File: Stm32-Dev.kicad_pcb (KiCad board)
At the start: 2 copper layers, 33 x 92.7 mm, 37 parts, among them J2 STDC14, U1 STM32F405RGTx, U2 TPS63070RNMR, X1 25MHz

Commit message: PCB ready for routing
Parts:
- moved S2 0.86 mm to (159.2, 86.2)
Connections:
- S2 pad S1: (no net) -> GND
- S2 pad S2: (no net) -> GND
- S2 pad S3: (no net) -> GND
- S2 pad S4: (no net) -> GND
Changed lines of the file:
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@@
   )
   (footprint "EG1215AA:SW_EG1215AA" (layer "F.Cu")
-    (at 160.02 86.13 -90)
+    (at 159.165 86.2 -90)
     (property "MANUFACTURER" "E Switch")
     (property "MAXIMUM_PACKAGE_HEIGHT" "1.40mm")
@@
     (property "Sheetname" "")
     (attr smd)
-    (fp_text reference "S2" (at -1.225 -4.131 -90) (layer "F.SilkS")
+    (fp_text reference "S2" (at -1.225 -4.131 90) (layer "F.SilkS")
         (effects (font (size 1 1) (thickness 0.15)))
     )
-    (fp_text value "BOOT0" (at 2.585 4.077 -90) (layer "F.Fab")
+    (fp_text value "BOOT0" (at 2.585 4.077 90) (layer "F.Fab")
         (effects (font (size 1 1) (thickness 0.15)))
     )
@@
     (pad "3" smd rect (at 2.25 -1.75 270) (size 0.7 1.5) (layers "F.Cu" "F.Paste" "F.Mask")
       (net 2 "GND") (pintype "passive"))
-    (pad "S1" smd rect (at -3.65 -1.05 270) (size 1 0.8) (layers "F.Cu" "F.Paste" "F.Mask"))
-    (pad "S2" smd rect (at -3.65 1.05 270) (size 1 0.8) (layers "F.Cu" "F.Paste" "F.Mask"))
-    (pad "S3" smd rect (at 3.65 1.05 270) (size 1 0.8) (layers "F.Cu" "F.Paste" "F.Mask"))
-    (pad "S4" smd rect (at 3.65 -1.05 270) (size 1 0.8) (layers "F.Cu" "F.Paste" "F.Mask"))
+    (pad "S1" smd rect (at -3.65 -1.05 270) (size 1 0.8) (layers "F.Cu" "F.Paste" "F.Mask")
+      (net 2 "GND"))
+    (pad "S2" smd rect (at -3.65 1.05 270) (size 1 0.8) (layers "F.Cu" "F.Paste" "F.Mask")
+      (net 2 "GND"))
+    (pad "S3" smd rect (at 3.65 1.05 270) (size 1 0.8) (layers "F.Cu" "F.Paste" "F.Mask")
+      (net 2 "GND"))
+    (pad "S4" smd rect (at 3.65 -1.05 270) (size 1 0.8) (layers "F.Cu" "F.Paste" "F.Mask")
+      (net 2 "GND"))
   )
   (footprint "Package_QFP:LQFP-64_10x10mm_P0.5mm" (layer "F.Cu")

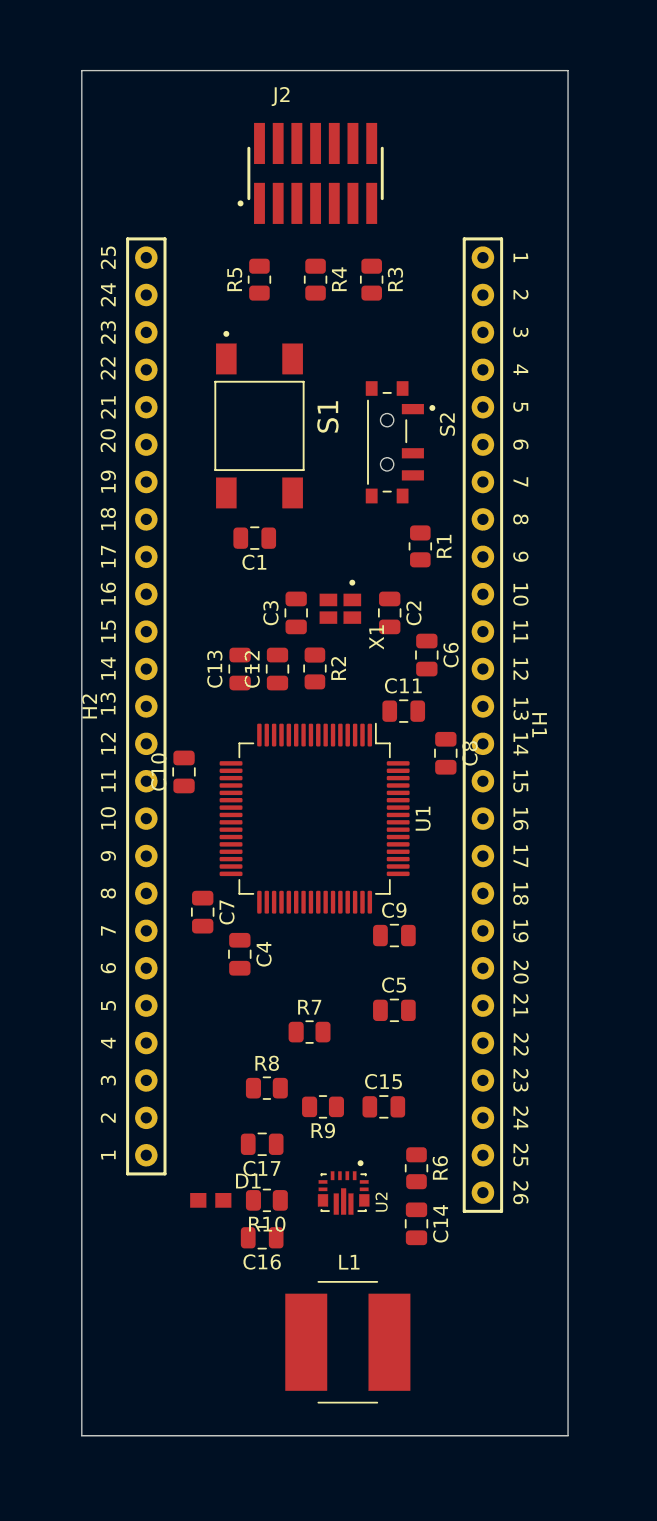
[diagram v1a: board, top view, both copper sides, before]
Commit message: Changed Boot Switch
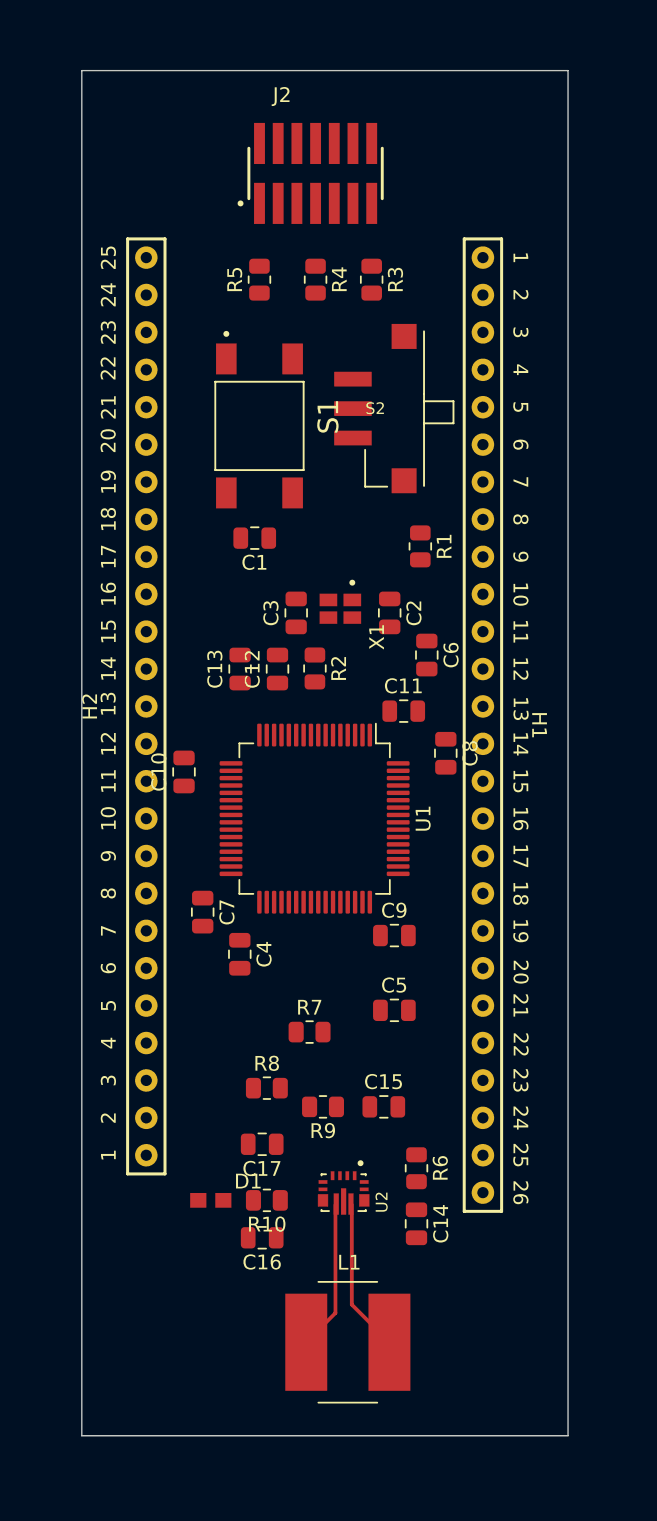
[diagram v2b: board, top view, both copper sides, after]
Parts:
- S2: value BOOT0 -> SS312SAH4-R; footprint EG1215AA:SW_EG1215AA -> SS312SAH4-R:SW_SS312SAH4-R
- moved S2 2.42 mm to (158.4, 83.9), turned to 180 degrees
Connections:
- S2 pad 1: VDD -> GND
- S2 pad 3: GND -> VDD
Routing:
- net Net-(U2-L1): track 0.00 -> 10.4 mm
- net Net-(U2-L2): track 0.00 -> 10.2 mm
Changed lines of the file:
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@@
     )
   )
-  (footprint "EG1215AA:SW_EG1215AA" (layer "F.Cu")
-    (at 159.165 86.2 -90)
-    (property "MANUFACTURER" "E Switch")
-    (property "MAXIMUM_PACKAGE_HEIGHT" "1.40mm")
-    (property "PARTREV" "A")
-    (property "STANDARD" "Manufacturer Recommendations")
+  (footprint "SS312SAH4-R:SW_SS312SAH4-R" (layer "F.Cu")
+    (at 158.37 83.915 180)
+    (property "MANUFACTURER" "NKK switches")
     (property "Sheetfile" "Stm32-Dev.kicad_sch")
     (property "Sheetname" "")
     (attr smd)
-    (fp_text reference "S2" (at -1.225 -4.131 90) (layer "F.SilkS")
-        (effects (font (size 1 1) (thickness 0.15)))
-    )
-    (fp_text value "BOOT0" (at 2.585 4.077 90) (layer "F.Fab")
-        (effects (font (size 1 1) (thickness 0.15)))
-    )
-    (fp_line (start -3.35 -0.254) (end -3.35 0.254)
-      (stroke (width 0.127) (type solid)) (layer "F.SilkS"))
-    (fp_line (start -2.83 1.3) (end 2.83 1.3)
-      (stroke (width 0.127) (type solid)) (layer "F.SilkS"))
-    (fp_line (start -1.5 -1.3) (end 0 -1.3)
-      (stroke (width 0.127) (type solid)) (layer "F.SilkS"))
-    (fp_line (start 3.35 -0.254) (end 3.35 0.254)
-      (stroke (width 0.127) (type solid)) (layer "F.SilkS"))
-    (fp_circle (center -2.329 -3.071) (end -2.229 -3.071)
-      (stroke (width 0.2) (type solid)) (fill none) (layer "F.SilkS"))
-    (fp_line (start -4.4 -2.75) (end -4.4 2.95)
-      (stroke (width 0.05) (type solid)) (layer "F.CrtYd"))
-    (fp_line (start -4.4 2.95) (end 4.4 2.95)
-      (stroke (width 0.05) (type solid)) (layer "F.CrtYd"))
-    (fp_line (start 4.4 -2.75) (end -4.4 -2.75)
-      (stroke (width 0.05) (type solid)) (layer "F.CrtYd"))
-    (fp_line (start 4.4 2.95) (end 4.4 -2.75)
-      (stroke (width 0.05) (type solid)) (layer "F.CrtYd"))
-    (fp_line (start -3.35 -1.3) (end 3.35 -1.3)
+    (fp_text reference "S2" (at 0 0) (layer "F.SilkS")
+        (effects (font (size 0.787402 0.787402) (thickness 0.15)))
+    )
+    (fp_text value "SS312SAH4-R" (at 0 0) (layer "F.Fab")
+        (effects (font (size 0.787402 0.787402) (thickness 0.15)))
+    )
+    (fp_line (start -5.3 -1) (end -5.3 0.5)
+      (stroke (width 0.127) (type solid)) (layer "F.SilkS"))
+    (fp_line (start -5.3 0.5) (end -3.3 0.5)
+      (stroke (width 0.127) (type solid)) (layer "F.SilkS"))
+    (fp_line (start -3.3 -5.25) (end -3.3 -1)
+      (stroke (width 0.127) (type solid)) (layer "F.SilkS"))
+    (fp_line (start -3.3 -1) (end -5.3 -1)
+      (stroke (width 0.127) (type solid)) (layer "F.SilkS"))
+    (fp_line (start -3.3 -1) (end -3.3 0.5)
+      (stroke (width 0.127) (type solid)) (layer "F.SilkS"))
+    (fp_line (start -3.3 0.5) (end -3.3 1)
+      (stroke (width 0.127) (type solid)) (layer "F.SilkS"))
+    (fp_line (start -3.3 1) (end -3.3 5.25)
+      (stroke (width 0.127) (type solid)) (layer "F.SilkS"))
+    (fp_line (start -0.8 -5.3) (end 0.7 -5.3)
+      (stroke (width 0.127) (type solid)) (layer "F.SilkS"))
+    (fp_line (start 0.7 -5.3) (end 0.7 -2.8)
+      (stroke (width 0.127) (type solid)) (layer "F.SilkS"))
+    (fp_line (start -5.6 -1.3) (end -5.6 1.3)
+      (stroke (width 0.127) (type solid)) (layer "F.CrtYd"))
+    (fp_line (start -5.6 1.3) (end -3.6 1.3)
+      (stroke (width 0.127) (type solid)) (layer "F.CrtYd"))
+    (fp_line (start -3.7 -6) (end -3.7 -1.3)
+      (stroke (width 0.127) (type solid)) (layer "F.CrtYd"))
+    (fp_line (start -3.7 -6) (end 1 -6)
+      (stroke (width 0.127) (type solid)) (layer "F.CrtYd"))
+    (fp_line (start -3.7 -1.3) (end -5.6 -1.3)
+      (stroke (width 0.127) (type solid)) (layer "F.CrtYd"))
+    (fp_line (start -3.6 1.3) (end -3.6 6)
+      (stroke (width 0.127) (type solid)) (layer "F.CrtYd"))
+    (fp_line (start -3.6 6) (end 1 6)
+      (stroke (width 0.127) (type solid)) (layer "F.CrtYd"))
+    (fp_line (start 1 -6) (end 1 -2.8)
+      (stroke (width 0.127) (type solid)) (layer "F.CrtYd"))
+    (fp_line (start 1 2.8) (end 3.1 2.8)
+      (stroke (width 0.127) (type solid)) (layer "F.CrtYd"))
+    (fp_line (start 1 6) (end 1 2.8)
+      (stroke (width 0.127) (type solid)) (layer "F.CrtYd"))
+    (fp_line (start 3.1 -2.8) (end 1 -2.8)
+      (stroke (width 0.127) (type solid)) (layer "F.CrtYd"))
+    (fp_line (start 3.1 2.8) (end 3.1 -2.8)
+      (stroke (width 0.127) (type solid)) (layer "F.CrtYd"))
+    (fp_line (start -3.1 5.3) (end -0.8 5.3)
       (stroke (width 0.127) (type solid)) (layer "F.Fab"))
-    (fp_line (start -3.35 1.3) (end -3.35 -1.3)
+    (fp_line (start -3 -5.3) (end -0.8 -5.3)
       (stroke (width 0.127) (type solid)) (layer "F.Fab"))
-    (fp_line (start 0.1 1.3) (end -3.35 1.3)
+    (fp_line (start 0.7 -2.8) (end 0.7 2.9)
       (stroke (width 0.127) (type solid)) (layer "F.Fab"))
-    (fp_line (start 0.1 1.3) (end 0.1 2.7)
-      (stroke (width 0.127) (type solid)) (layer "F.Fab"))
-    (fp_line (start 0.1 1.3) (end 1.4 1.3)
-      (stroke (width 0.127) (type solid)) (layer "F.Fab"))
-    (fp_line (start 0.1 2.7) (end 1.4 2.7)
-      (stroke (width 0.127) (type solid)) (layer "F.Fab"))
-    (fp_line (start 1.4 2.7) (end 1.4 1.3)
-      (stroke (width 0.127) (type solid)) (layer "F.Fab"))
-    (fp_line (start 3.35 -1.3) (end 3.35 1.3)
-      (stroke (width 0.127) (type solid)) (layer "F.Fab"))
-    (fp_line (start 3.35 1.3) (end 1.4 1.3)
-      (stroke (width 0.127) (type solid)) (layer "F.Fab"))
-    (fp_circle (center -2.329 -3.071) (end -2.229 -3.071)
-      (stroke (width 0.2) (type solid)) (fill none) (layer "F.Fab"))
-    (pad "" np_thru_hole circle (at -1.5 0 270) (size 0.9 0.9) (drill 0.9) (layers "*.Cu" "*.Mask"))
-    (pad "" np_thru_hole circle (at 1.5 0 270) (size 0.9 0.9) (drill 0.9) (layers "*.Cu" "*.Mask"))
-    (pad "1" smd rect (at -2.25 -1.75 270) (size 0.7 1.5) (layers "F.Cu" "F.Paste" "F.Mask")
-      (net 7 "VDD") (pintype "passive"))
-    (pad "2" smd rect (at 0.75 -1.75 270) (size 0.7 1.5) (layers "F.Cu" "F.Paste" "F.Mask")
-      (net 69 "Net-(R1-Pad1)") (pintype "passive"))
-    (pad "3" smd rect (at 2.25 -1.75 270) (size 0.7 1.5) (layers "F.Cu" "F.Paste" "F.Mask")
-      (net 2 "GND") (pintype "passive"))
-    (pad "S1" smd rect (at -3.65 -1.05 270) (size 1 0.8) (layers "F.Cu" "F.Paste" "F.Mask")
-      (net 2 "GND"))
-    (pad "S2" smd rect (at -3.65 1.05 270) (size 1 0.8) (layers "F.Cu" "F.Paste" "F.Mask")
-      (net 2 "GND"))
-    (pad "S3" smd rect (at 3.65 1.05 270) (size 1 0.8) (layers "F.Cu" "F.Paste" "F.Mask")
-      (net 2 "GND"))
-    (pad "S4" smd rect (at 3.65 -1.05 270) (size 1 0.8) (layers "F.Cu" "F.Paste" "F.Mask")
-      (net 2 "GND"))
+    (fp_poly
+      (pts
+        (xy 0.700254 1.7)
+        (xy 2.6 1.7)
+        (xy 2.6 2.30083)
+        (xy 0.700254 2.30083)
+      )
+      (stroke (width 0.01) (type solid)) (fill solid) (layer "F.Fab"))
+    (fp_poly
+      (pts
+        (xy 0.700741 -2.3)
+        (xy 2.6 -2.3)
+        (xy 2.6 -1.7018)
+        (xy 0.700741 -1.7018)
+      )
+      (stroke (width 0.01) (type solid)) (fill solid) (layer "F.Fab"))
+    (fp_poly
+      (pts
+        (xy 0.700768 -0.3)
+        (xy 2.6 -0.3)
+        (xy 2.6 0.300329)
+        (xy 0.700768 0.300329)
+      )
+      (stroke (width 0.01) (type solid)) (fill solid) (layer "F.Fab"))
+    (pad "1" smd rect (at 1.525 2 180) (size 2.55 1) (layers "F.Cu" "F.Paste" "F.Mask")
+      (net 2 "GND") (pinfunction "1") (pintype "passive"))
+    (pad "2" smd rect (at 1.525 0 180) (size 2.55 1) (layers "F.Cu" "F.Paste" "F.Mask")
+      (net 69 "Net-(R1-Pad1)") (pinfunction "2") (pintype "passive"))
+    (pad "3" smd rect (at 1.525 -2 180) (size 2.55 1) (layers "F.Cu" "F.Paste" "F.Mask")
+      (net 7 "VDD") (pinfunction "3") (pintype "passive"))
+    (pad "P$1" smd rect (at -1.95 4.9 180) (size 1.7 1.7) (layers "F.Cu" "F.Paste" "F.Mask"))
+    (pad "P$2" smd rect (at -1.95 -4.9 180) (size 1.7 1.7) (layers "F.Cu" "F.Paste" "F.Mask"))
   )
   (footprint "Package_QFP:LQFP-64_10x10mm_P0.5mm" (layer "F.Cu")
@@
   (gr_line (start 171.45 153.67) (end 138.43 153.67)
     (stroke (width 0.0254) (type default)) (layer "Edge.Cuts"))
+  (segment (start 155.654 145.336) (end 155.654 137.991) (width 0.254) (layer "F.Cu") (net 67))
+  (segment (start 153.67 147.32) (end 155.654 145.336) (width 0.254) (layer "F.Cu") (net 67))
+  (segment (start 159.32 147.32) (end 156.766 144.766) (width 0.254) (layer "F.Cu") (net 68))
+  (segment (start 156.766 144.766) (end 156.766 137.991) (width 0.254) (layer "F.Cu") (net 68))
 )

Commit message: First Test Board
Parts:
- H1: footprint 24_PIN_HEADER:HDRV26 -> 24_PIN_HEADER:HDRV16
- H2: footprint 24_PIN_HEADER:HDRV25 -> 24_PIN_HEADER:HDRV16
- moved H1 24.7 mm to (141.0, 105.4)
- moved H2 23.6 mm to (166.4, 105.4), turned to -90 degrees
- moved C4 8.28 mm to (145.0, 113.8), turned to 90 degrees
- moved C5 4.82 mm to (156.2, 121.4), turned to -90 degrees
- moved X1 2.57 mm to (155.6, 100.0)
- moved C2 2.56 mm to (157.1, 96.5)
- moved C3 2.04 mm to (154.6, 96.5)
- moved R2 1.85 mm to (155.6, 102.9), turned to 0 degrees
- moved C12 1.27 mm to (150.5, 101.9)
- moved C13 1.27 mm to (148.0, 101.9)
- moved C16 0.31 mm to (150.9, 140.5)
- moved C17 0.31 mm to (150.9, 134.1)
- moved R6 0.17 mm to (161.0, 135.4), turned to 90 degrees
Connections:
- H1 pad 1: GND -> Net-(U1-PD2)
- H1 pad 10: Net-(U1-PA15) -> Net-(U1-PC11)
- H1 pad 11: Net-(U1-PA14) -> Net-(U1-PC12)
- H1 pad 12: Net-(U1-PA13) -> Net-(U1-PB14)
- H1 pad 13: Net-(U1-PA12) -> Net-(U1-PB13)
- H1 pad 14: Net-(U1-PA11) -> Net-(U1-PB12)
- H1 pad 15: Net-(U1-PA10) -> Net-(U1-PB11)
- H1 pad 16: Net-(U1-PA9) -> Net-(U1-PB10)
- H1 pad 2: Net-(U1-PB7) -> Net-(U1-PC0)
- H1 pad 3: Net-(U1-PB6) -> Net-(U1-PC1)
- H1 pad 4: Net-(U1-PB5) -> Net-(U1-PC2)
- H1 pad 5: Net-(U1-PB4) -> Net-(U1-PC3)
- H1 pad 6: Net-(U1-PB3) -> Net-(U1-PC6)
- H1 pad 7: Net-(U1-PB2) -> Net-(U1-PC7)
- H1 pad 8: Net-(U1-PB1) -> Net-(U1-PC8)
- H1 pad 9: Net-(U1-PB0) -> Net-(U1-PC10)
- H2 pad 1: Net-(U1-PD2) -> GND
- H2 pad 10: Net-(U1-PC8) -> Net-(U1-PA4)
- H2 pad 11: Net-(U1-PC9) -> Net-(U1-PA3)
- H2 pad 12: Net-(U1-PC10) -> Net-(U1-PA2)
- H2 pad 13: Net-(U1-PC11) -> Net-(U1-PA1)
- H2 pad 14: Net-(U1-PC12) -> Net-(U1-PA0)
- H2 pad 15: Net-(U1-PC13) -> unconnected-(H2-Pad15)
- H2 pad 16: Net-(U1-PC14) -> +VDC
- H2 pad 2: Net-(U1-PC0) -> Net-(U1-PB7)
- H2 pad 3: Net-(U1-PC1) -> Net-(U1-PB6)
- H2 pad 4: Net-(U1-PC2) -> Net-(U1-PA11)
- H2 pad 5: Net-(U1-PC3) -> Net-(U1-PA10)
- H2 pad 6: Net-(U1-PC4) -> Net-(U1-PA9)
- H2 pad 7: Net-(U1-PC5) -> Net-(U1-PA8)
- H2 pad 8: Net-(U1-PC6) -> Net-(U1-PA6)
- H2 pad 9: Net-(U1-PC7) -> Net-(U1-PA5)
- U1 pad 2: Net-(U1-PC13) -> unconnected-(U1-PC13-Pad2)
- U1 pad 23: Net-(U1-PA7) -> unconnected-(U1-PA7-Pad23)
- U1 pad 24: Net-(U1-PC4) -> unconnected-(U1-PC4-Pad24)
- U1 pad 25: Net-(U1-PC5) -> unconnected-(U1-PC5-Pad25)
- U1 pad 26: Net-(U1-PB0) -> unconnected-(U1-PB0-Pad26)
- U1 pad 27: Net-(U1-PB1) -> unconnected-(U1-PB1-Pad27)
- U1 pad 28: Net-(U1-PB2) -> unconnected-(U1-PB2-Pad28)
- U1 pad 3: Net-(U1-PC14) -> unconnected-(U1-PC14-Pad3)
- U1 pad 36: Net-(U1-PB15) -> unconnected-(U1-PB15-Pad36)
- U1 pad 4: Net-(U1-PC15) -> unconnected-(U1-PC15-Pad4)
- U1 pad 40: Net-(U1-PC9) -> unconnected-(U1-PC9-Pad40)
- U1 pad 45: Net-(U1-PA12) -> unconnected-(U1-PA12-Pad45)
- U1 pad 50: Net-(U1-PA15) -> unconnected-(U1-PA15-Pad50)
- U1 pad 56: Net-(U1-PB4) -> unconnected-(U1-PB4-Pad56)
- U1 pad 57: Net-(U1-PB5) -> unconnected-(U1-PB5-Pad57)
- U1 pad 61: Net-(U1-PB8) -> unconnected-(U1-PB8-Pad61)
- U1 pad 62: Net-(U1-PB9) -> unconnected-(U1-PB9-Pad62)
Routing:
- net GND: track 0.00 -> 313.2 mm, vias 0 -> 3
- net VDD: track 0.00 -> 155.2 mm
- net Net-(U1-PC12): track 0.00 -> 91.3 mm, vias 0 -> 2
- net Net-(U1-PC10): track 0.00 -> 86.5 mm, vias 0 -> 2
- net Net-(U1-PA14): track 0.00 -> 69.6 mm, vias 0 -> 2
- net Net-(U1-PA13): track 0.00 -> 65.7 mm, vias 0 -> 2
- net Net-(U1-PB3): track 0.00 -> 64.0 mm
- net Net-(U1-PC11): track 0.00 -> 59.4 mm, vias 0 -> 3
- net Net-(U1-NRST): track 0.00 -> 49.3 mm, vias 0 -> 2
- net +VDC: track 0.00 -> 42.0 mm, vias 0 -> 1
- net Net-(U1-PA6): track 0.00 -> 39.6 mm, vias 0 -> 1
- net Net-(U1-PD2): track 0.00 -> 39.0 mm, vias 0 -> 1
- net Net-(U1-PA11): track 0.00 -> 37.9 mm, vias 0 -> 1
- net Net-(U1-PA1): track 0.00 -> 37.8 mm, vias 0 -> 2
- net Net-(U1-PA4): track 0.00 -> 28.1 mm, vias 0 -> 1
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- added copper zone on B.Cu, net GND
- added copper zone on F.Cu, net GND
